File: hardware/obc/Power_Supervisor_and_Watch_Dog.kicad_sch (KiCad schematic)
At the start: 23 parts, among them J201 Conn_01x02, Q51 IRF7306, Q52 PMBT2222A, Q53 MBT2222ADW1T1, Q54 MBT2222ADW1T1

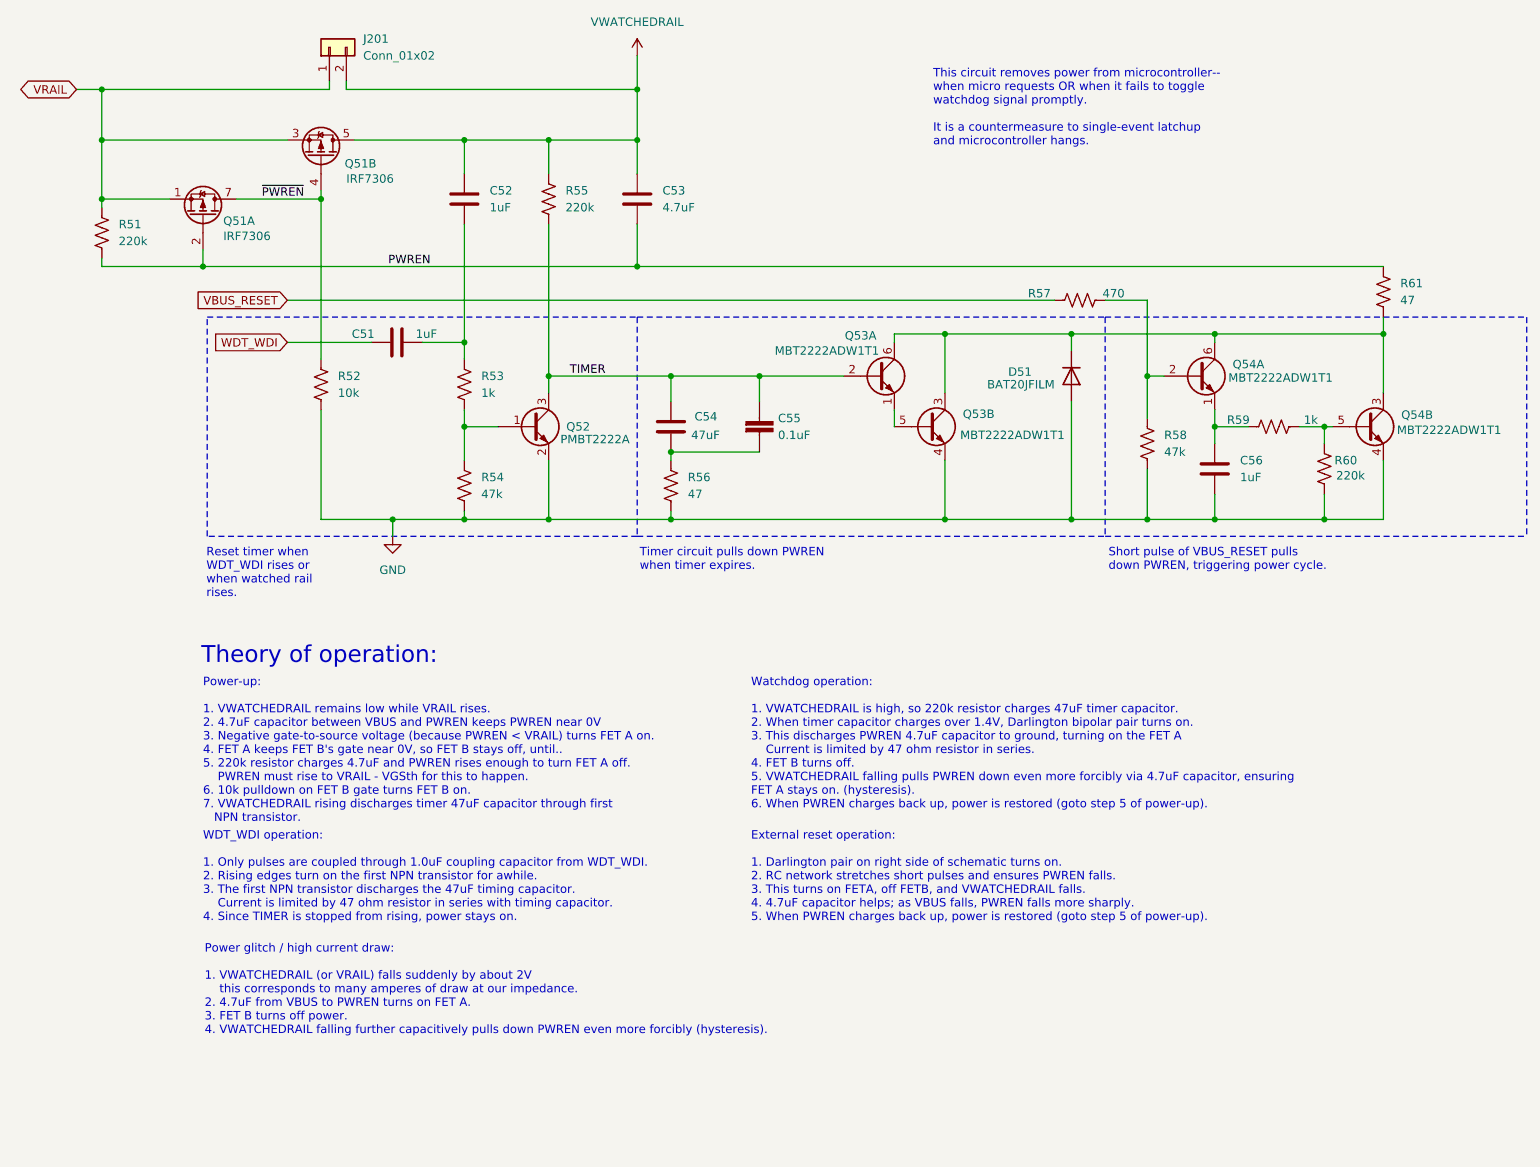
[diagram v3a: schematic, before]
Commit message: obc: design review and corrections
- text cleanup, put components on grid
- Re-route RF power network for radio to get thicker traces and lower
impedance.
- Route RF connections for GPS (controlled impedance)
- Lots of straightening and spreading traces and improving pours
(especially power paths).
- Swap pinning of RBF jumper to reduce the possible downsides of
any shorts or misconnections (don't put pack+ and pack- together on
the connector)
- geographical reannotate
- improve placement of a couple of bypass caps
- Adjust 10uF solar input capacitors to be 35V rated so as to not
limit input voltage.
- fix pinning of RF splitter
- add a couple of STEP models
- obc: add DQ1225 step model
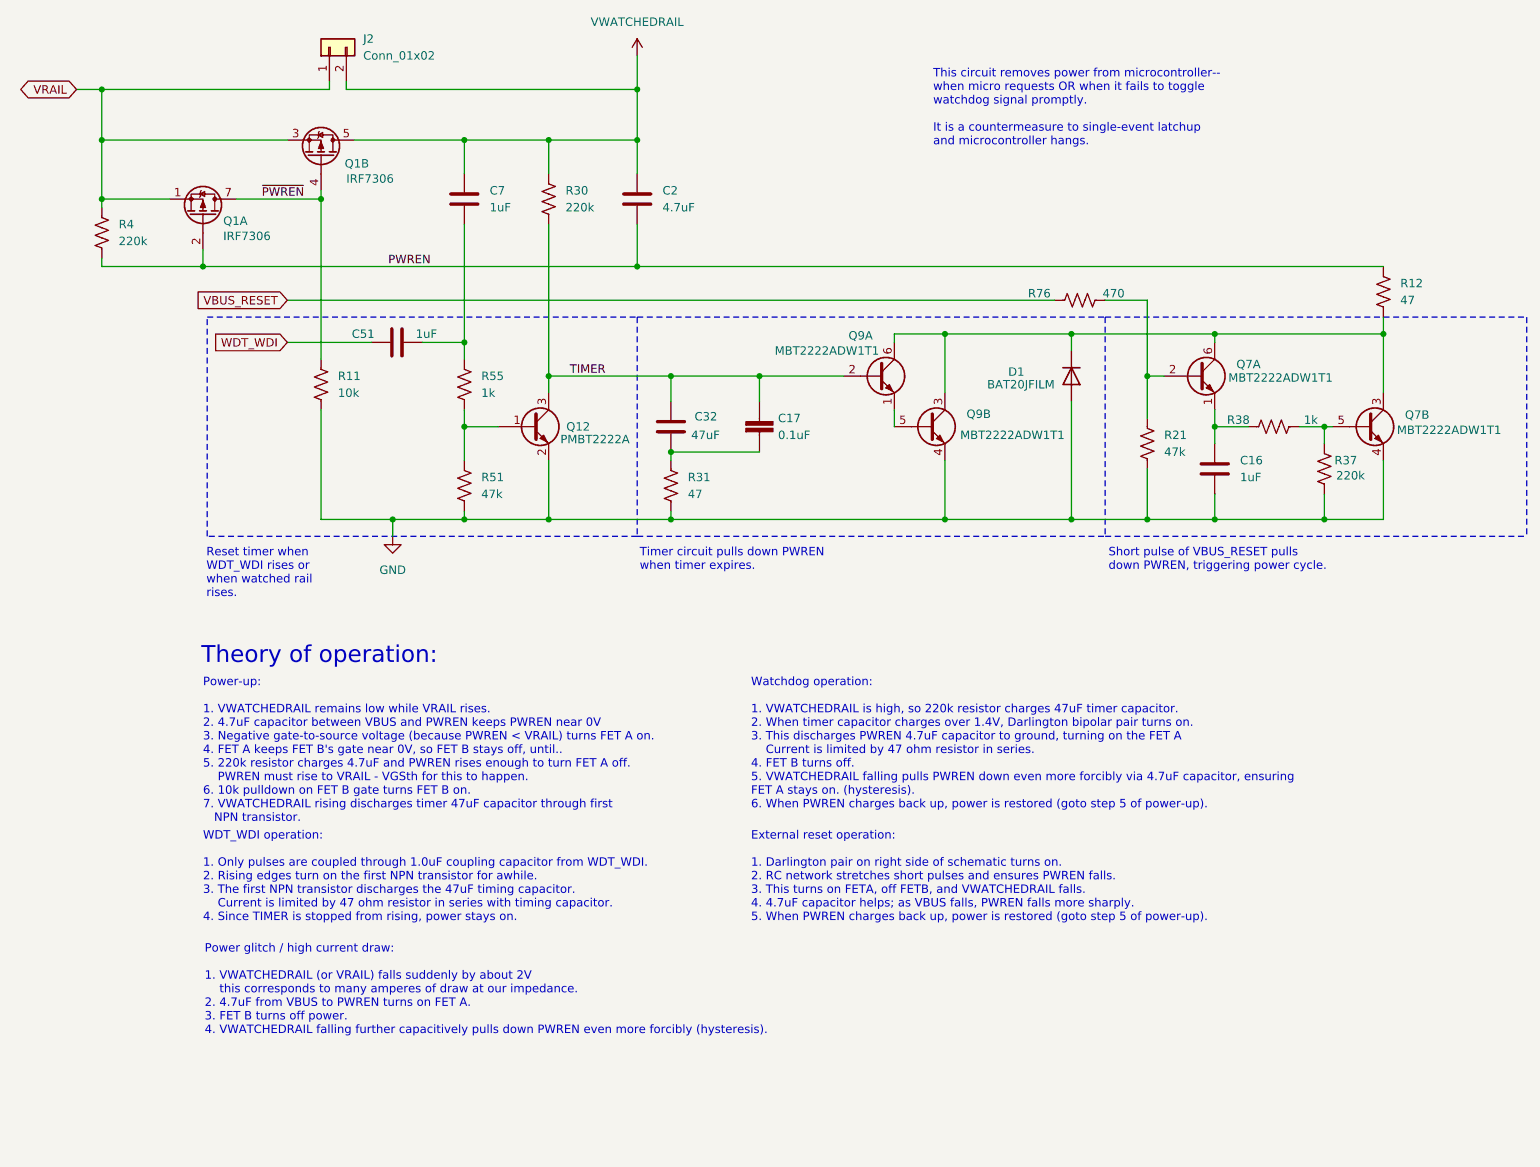
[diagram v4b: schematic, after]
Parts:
- C2: renamed from C53; LCSC C19666 -> C19666
- renumbered C56 to C16, C55 to C17, C54 to C32, C52 to C7, D51 to D1, J201 to J2, Q51 to Q1, Q52 to Q12, Q54 to Q7, Q53 to Q9, R52 to R11, R61 to R12, R58 to R21, R55 to R30, R56 to R31, R60 to R37, R59 to R38, R51 to R4, R54 to R51, R53 to R55, R57 to R76
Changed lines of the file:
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@@
 		(on_board yes)
 		(dnp no)
-		(property "Reference" "R59"
+		(property "Reference" "R38"
 			(at 200.406 76.454 90)
 			(effects
@@
 			(project "mainboard"
 				(path "/e3ac22ea-6806-4807-a025-571315789c25/0ba89562-211f-497f-9372-6f77bd1df388"
-					(reference "R59")
+					(reference "R38")
 					(unit 1)
 				)
@@
 		(dnp no)
 		(fields_autoplaced yes)
-		(property "Reference" "R53"
+		(property "Reference" "R55"
 			(at 86.36 69.8499 0)
 			(effects
@@
 			(project "mainboard"
 				(path "/e3ac22ea-6806-4807-a025-571315789c25/0ba89562-211f-497f-9372-6f77bd1df388"
-					(reference "R53")
+					(reference "R55")
 					(unit 1)
 				)
@@
 		(dnp no)
 		(fields_autoplaced yes)
-		(property "Reference" "C52"
+		(property "Reference" "C7"
 			(at 87.63 41.9099 0)
 			(effects
@@
 			(project "mainboard"
 				(path "/e3ac22ea-6806-4807-a025-571315789c25/0ba89562-211f-497f-9372-6f77bd1df388"
-					(reference "C52")
+					(reference "C7")
 					(unit 1)
 				)
@@
 		(dnp no)
 		(fields_autoplaced yes)
-		(property "Reference" "C56"
+		(property "Reference" "C16"
 			(at 200.66 82.5499 0)
 			(effects
@@
 			(project "mainboard"
 				(path "/e3ac22ea-6806-4807-a025-571315789c25/0ba89562-211f-497f-9372-6f77bd1df388"
-					(reference "C56")
+					(reference "C16")
 					(unit 1)
 				)
@@
 		(on_board yes)
 		(dnp no)
-		(property "Reference" "Q53"
+		(property "Reference" "Q9"
 			(at 143.51 63.754 0)
 			(effects
@@
 			(project "mainboard"
 				(path "/e3ac22ea-6806-4807-a025-571315789c25/0ba89562-211f-497f-9372-6f77bd1df388"
-					(reference "Q53")
+					(reference "Q9")
 					(unit 1)
 				)
@@
 		(dnp no)
 		(fields_autoplaced yes)
-		(property "Reference" "R51"
+		(property "Reference" "R4"
 			(at 31.75 46.9899 0)
 			(effects
@@
 			(project "mainboard"
 				(path "/e3ac22ea-6806-4807-a025-571315789c25/0ba89562-211f-497f-9372-6f77bd1df388"
-					(reference "R51")
+					(reference "R4")
 					(unit 1)
 				)
@@
 		(dnp no)
 		(fields_autoplaced yes)
-		(property "Reference" "R56"
+		(property "Reference" "R31"
 			(at 117.475 85.0899 0)
 			(effects
@@
 			(project "mainboard"
 				(path "/e3ac22ea-6806-4807-a025-571315789c25/0ba89562-211f-497f-9372-6f77bd1df388"
-					(reference "R56")
+					(reference "R31")
 					(unit 1)
 				)
@@
 		(on_board yes)
 		(dnp no)
-		(property "Reference" "D51"
+		(property "Reference" "D1"
 			(at 165.735 69.215 90)
 			(effects
@@
 			(project "mainboard"
 				(path "/e3ac22ea-6806-4807-a025-571315789c25/0ba89562-211f-497f-9372-6f77bd1df388"
-					(reference "D51")
+					(reference "D1")
 					(unit 1)
 				)
@@
 		(on_board yes)
 		(dnp no)
-		(property "Reference" "R52"
+		(property "Reference" "R11"
 			(at 64.77 69.8499 0)
 			(effects
@@
 			(project "mainboard"
 				(path "/e3ac22ea-6806-4807-a025-571315789c25/0ba89562-211f-497f-9372-6f77bd1df388"
-					(reference "R52")
+					(reference "R11")
 					(unit 1)
 				)
@@
 		(on_board yes)
 		(dnp no)
-		(property "Reference" "R55"
+		(property "Reference" "R30"
 			(at 99.06 41.9099 0)
 			(effects
@@
 			(project "mainboard"
 				(path "/e3ac22ea-6806-4807-a025-571315789c25/0ba89562-211f-497f-9372-6f77bd1df388"
-					(reference "R55")
+					(reference "R30")
 					(unit 1)
 				)
@@
 		(on_board yes)
 		(dnp no)
-		(property "Reference" "R57"
+		(property "Reference" "R76"
 			(at 170.434 57.404 90)
 			(effects
@@
 			(project "mainboard"
 				(path "/e3ac22ea-6806-4807-a025-571315789c25/0ba89562-211f-497f-9372-6f77bd1df388"
-					(reference "R57")
+					(reference "R76")
 					(unit 1)
 				)
@@
 		(on_board yes)
 		(dnp no)
-		(property "Reference" "Q52"
+		(property "Reference" "Q12"
 			(at 100.965 77.47 0)
 			(effects
@@
 			(project "mainboard"
 				(path "/e3ac22ea-6806-4807-a025-571315789c25/0ba89562-211f-497f-9372-6f77bd1df388"
-					(reference "Q52")
+					(reference "Q12")
 					(unit 1)
 				)
@@
 		(dnp no)
 		(fields_autoplaced yes)
-		(property "Reference" "R58"
+		(property "Reference" "R21"
 			(at 189.23 78.7399 0)
 			(effects
@@
 			(project "mainboard"
 				(path "/e3ac22ea-6806-4807-a025-571315789c25/0ba89562-211f-497f-9372-6f77bd1df388"
-					(reference "R58")
+					(reference "R21")
 					(unit 1)
 				)
@@
 		(dnp no)
 		(fields_autoplaced yes)
-		(property "Reference" "C53"
+		(property "Reference" "C2"
 			(at 113.665 41.9099 0)
 			(effects
@@
 			)
 		)
-		(property "LCSC" " C19666"
+		(property "LCSC" "C19666"
 			(at 109.855 43.18 0)
 			(effects
@@
 			(project "mainboard"
 				(path "/e3ac22ea-6806-4807-a025-571315789c25/0ba89562-211f-497f-9372-6f77bd1df388"
-					(reference "C53")
+					(reference "C2")
 					(unit 1)
 				)
@@
 		(dnp no)
 		(fields_autoplaced yes)
-		(property "Reference" "J201"
+		(property "Reference" "J2"
 			(at 68.58 19.0499 90)
 			(effects
@@
 			(project ""
 				(path "/e3ac22ea-6806-4807-a025-571315789c25/0ba89562-211f-497f-9372-6f77bd1df388"
-					(reference "J201")
+					(reference "J2")
 					(unit 1)
 				)
@@
 		(on_board yes)
 		(dnp no)
-		(property "Reference" "R61"
+		(property "Reference" "R12"
 			(at 224.79 55.8799 0)
 			(effects
@@
 			(project "mainboard"
 				(path "/e3ac22ea-6806-4807-a025-571315789c25/0ba89562-211f-497f-9372-6f77bd1df388"
-					(reference "R61")
+					(reference "R12")
 					(unit 1)
 				)
@@
 		(on_board yes)
 		(dnp no)
-		(property "Reference" "C55"
+		(property "Reference" "C17"
 			(at 131.064 76.2 0)
 			(effects
@@
 			(project "mainboard"
 				(path "/e3ac22ea-6806-4807-a025-571315789c25/0ba89562-211f-497f-9372-6f77bd1df388"
-					(reference "C55")
+					(reference "C17")
 					(unit 1)
 				)
@@
 		(on_board yes)
 		(dnp no)
-		(property "Reference" "Q54"
+		(property "Reference" "Q7"
 			(at 227.33 75.692 0)
 			(effects
@@
 			(project "mainboard"
 				(path "/e3ac22ea-6806-4807-a025-571315789c25/0ba89562-211f-497f-9372-6f77bd1df388"
-					(reference "Q54")
+					(reference "Q7")
 					(unit 2)
 				)
@@
 		(on_board yes)
 		(dnp no)
-		(property "Reference" "C54"
+		(property "Reference" "C32"
 			(at 118.491 75.946 0)
 			(effects
@@
 			(project "mainboard"
 				(path "/e3ac22ea-6806-4807-a025-571315789c25/0ba89562-211f-497f-9372-6f77bd1df388"
-					(reference "C54")
+					(reference "C32")
 					(unit 1)
 				)
@@
 		(on_board yes)
 		(dnp no)
-		(property "Reference" "Q54"
+		(property "Reference" "Q7"
 			(at 201.93 68.072 0)
 			(effects
@@
 			(project "mainboard"
 				(path "/e3ac22ea-6806-4807-a025-571315789c25/0ba89562-211f-497f-9372-6f77bd1df388"
-					(reference "Q54")
+					(reference "Q7")
 					(unit 1)
 				)
@@
 		(dnp no)
 		(fields_autoplaced yes)
-		(property "Reference" "R54"
+		(property "Reference" "R51"
 			(at 86.36 85.0899 0)
 			(effects
@@
 			(project "mainboard"
 				(path "/e3ac22ea-6806-4807-a025-571315789c25/0ba89562-211f-497f-9372-6f77bd1df388"
-					(reference "R54")
+					(reference "R51")
 					(unit 1)
 				)
@@
 		(on_board yes)
 		(dnp no)
-		(property "Reference" "Q51"
+		(property "Reference" "Q1"
 			(at 47.498 46.482 90)
 			(effects
@@
 			(project "mainboard"
 				(path "/e3ac22ea-6806-4807-a025-571315789c25/0ba89562-211f-497f-9372-6f77bd1df388"
-					(reference "Q51")
+					(reference "Q1")
 					(unit 1)
 				)
@@
 		(on_board yes)
 		(dnp no)
-		(property "Reference" "Q53"
+		(property "Reference" "Q9"
 			(at 161.29 75.565 0)
 			(effects
@@
 			(project "mainboard"
 				(path "/e3ac22ea-6806-4807-a025-571315789c25/0ba89562-211f-497f-9372-6f77bd1df388"
-					(reference "Q53")
+					(reference "Q9")
 					(unit 2)
 				)
@@
 		(on_board yes)
 		(dnp no)
-		(property "Reference" "R60"
+		(property "Reference" "R37"
 			(at 214.884 82.55 0)
 			(effects
@@
 			(project "mainboard"
 				(path "/e3ac22ea-6806-4807-a025-571315789c25/0ba89562-211f-497f-9372-6f77bd1df388"
-					(reference "R60")
+					(reference "R37")
 					(unit 1)
 				)
@@
 		(on_board yes)
 		(dnp no)
-		(property "Reference" "Q51"
+		(property "Reference" "Q1"
 			(at 65.786 37.846 90)
 			(effects
@@
 			(project "mainboard"
 				(path "/e3ac22ea-6806-4807-a025-571315789c25/0ba89562-211f-497f-9372-6f77bd1df388"
-					(reference "Q51")
+					(reference "Q1")
 					(unit 2)
 				)
